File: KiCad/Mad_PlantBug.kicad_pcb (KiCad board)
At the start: 2 copper layers, 30 x 126.9 mm, 38 parts, among them IC1 TMP102AIDRLR, J2 Conn_01x03, Q1 AO3401A, Q2 YJL2302B, U1 YJ-14015, U2 TLV333IDBVR

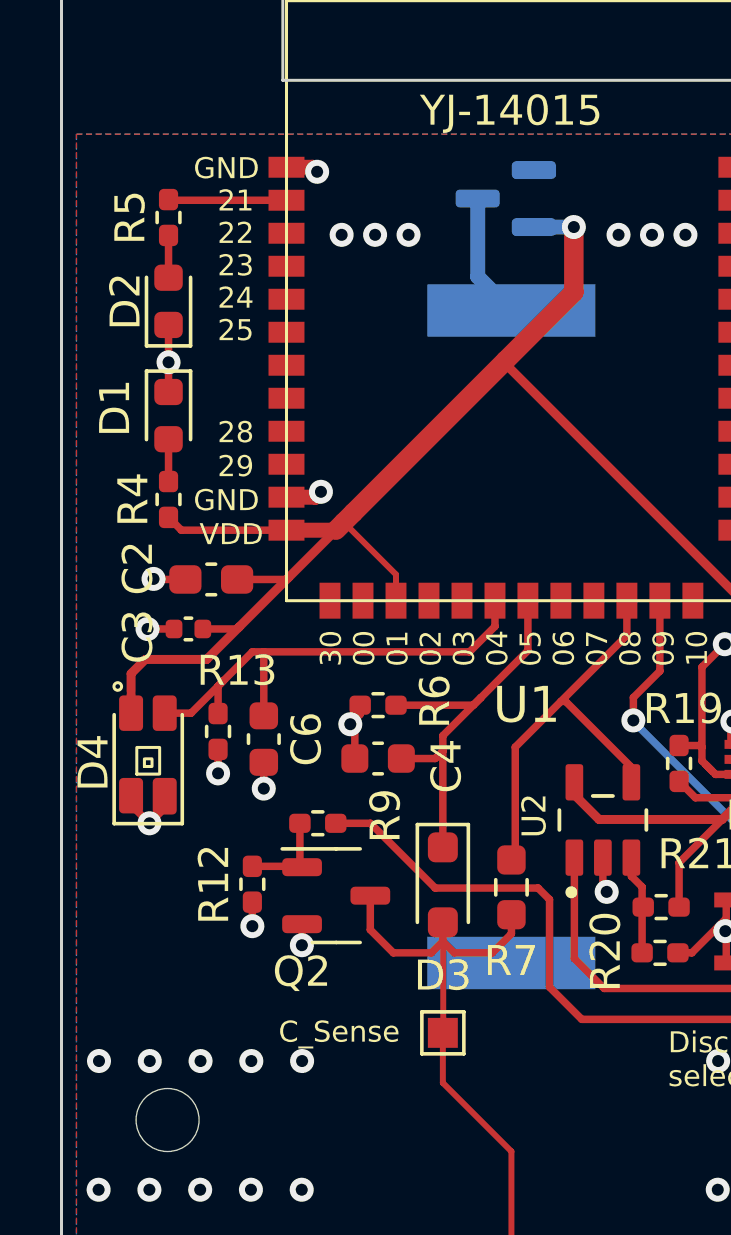
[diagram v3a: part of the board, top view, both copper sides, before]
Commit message: Routed UART, added some designators, added gerbers.
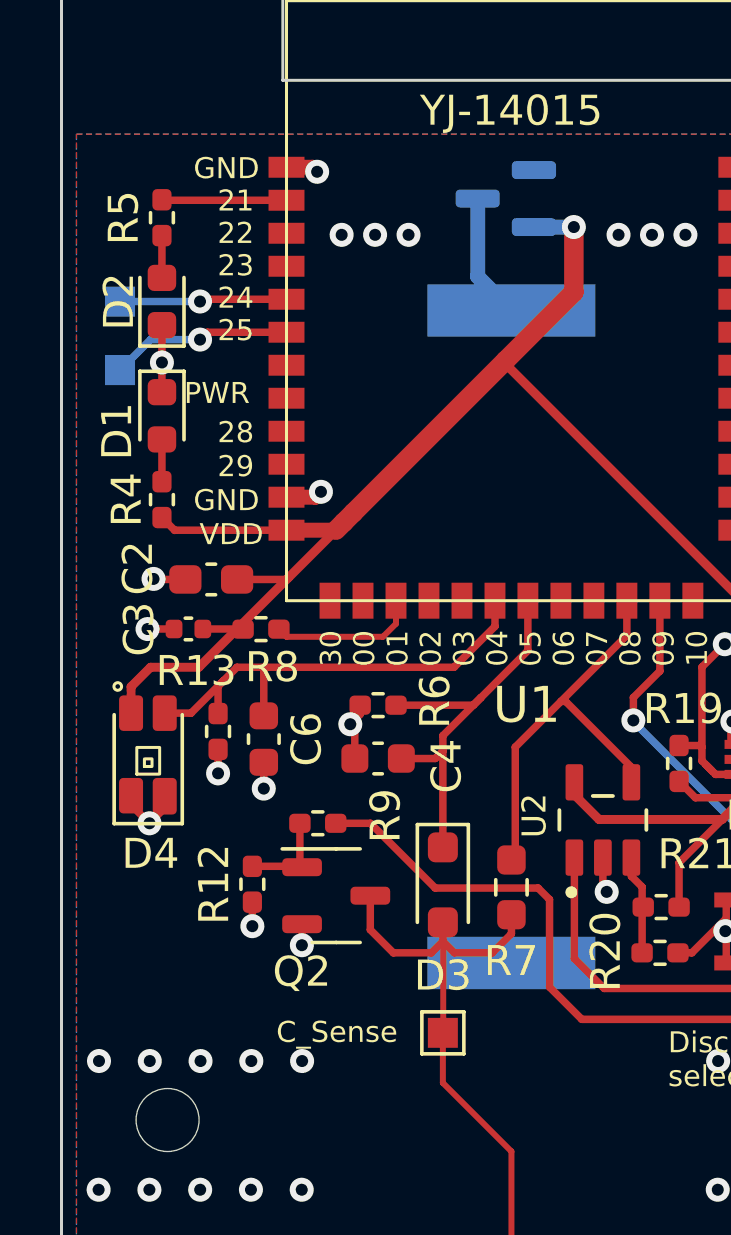
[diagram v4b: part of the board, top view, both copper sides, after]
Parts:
- added R8: R_protect, Resistor_SMD:R_0402_1005Metric_Pad0.72x0.64mm_HandSolder, F.Cu at (52.8, 51.8)
- added TP2: TXO, TestPoint:TestPoint_Pad_1.0x1.0mm, B.Cu at (48.1, 43.2)
- added TP3: RXI, TestPoint:TestPoint_Pad_1.0x1.0mm, B.Cu at (48.1, 40.9)
- moved D1 0.22 mm to (49.5, 44.7)
- moved R5 0.22 mm to (49.5, 38.1)
- moved D2 0.22 mm to (49.5, 40.9)
- moved R4 0.22 mm to (49.5, 47.5)
- renumbered C_Sense to TP1
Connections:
- C2 pad 1: PWR_SENSE -> VCC
- C3 pad 1: PWR_SENSE -> VCC
- C9 pad 1: PWR_SENSE -> VCC
- D4 pad 1: PWR_SENSE -> VCC
- IC1 pad 5: PWR_SENSE -> VCC
- Q1 pad 2: PWR_SENSE -> VCC
- R1 pad 1: PWR_SENSE -> VCC
- R18 pad 1: PWR_SENSE -> VCC
- R19 pad 1: PWR_SENSE -> VCC
- R21 pad 2: PWR_SENSE -> VCC
- R4 pad 1: PWR_SENSE -> VCC
- U1 pad 12: PWR_SENSE -> VCC
- U1 pad 5: unconnected-(U1-P24-Pad5) -> UART_RX
- U1 pad 6: unconnected-(U1-P25-Pad6) -> UART_TX
- U2 pad 5: PWR_SENSE -> VCC
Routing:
- net VCC: track 0.00 -> 77.3 mm, vias 0 -> 1
- net PWR_SENSE: track 80.7 -> 4.96 mm, vias 1 -> 0
- net UART_TX: track 0.00 -> 6.07 mm, vias 0 -> 1
- net UART_RX: track 0.00 -> 5.58 mm, vias 0 -> 1
- net LIGHT_SENSE: track 16.4 -> 15.9 mm
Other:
- board text added: "C_Sense"
- board text added: "PWR"
- board text added: "RXI"
- board text added: "TXO"
